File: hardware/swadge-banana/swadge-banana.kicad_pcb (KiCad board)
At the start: 2 copper layers, 85 x 173.2 mm, 46 parts, among them J1 USB_B_Micro, SW1 SW_SPDT, U1 AP1117-33, U2 ESP-13-WROOM-02D, U3 BUS_PCIexpress, U4 OLED_CONNECTOR, U5 QMA6981, U6 OLED_DISPLAY

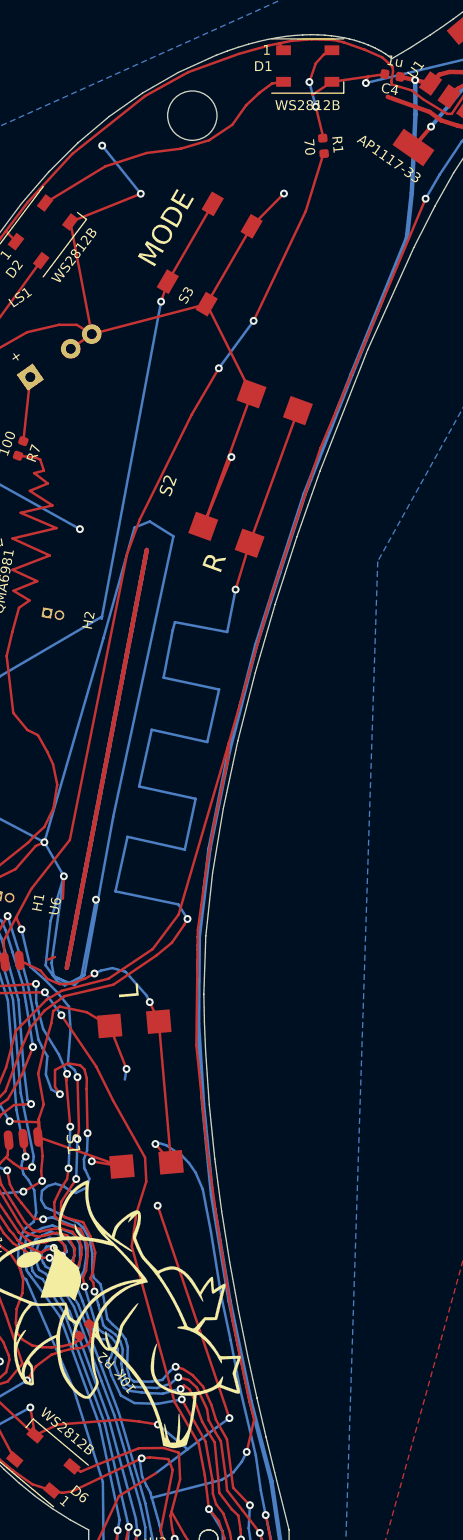
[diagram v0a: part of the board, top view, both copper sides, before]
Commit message: Readded missing batteries, filled zones
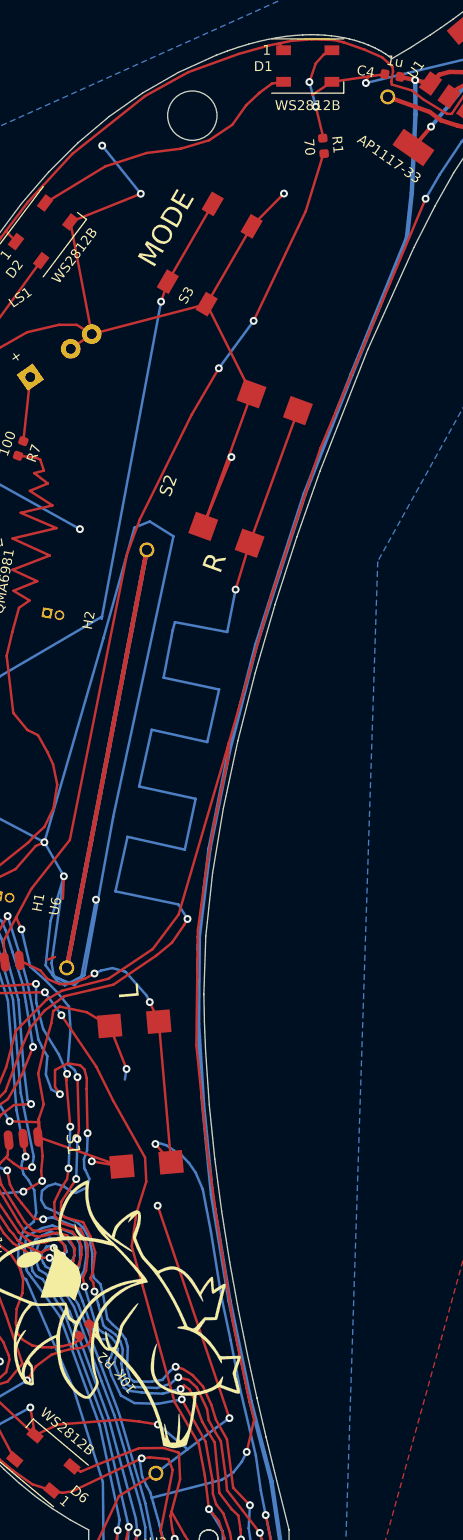
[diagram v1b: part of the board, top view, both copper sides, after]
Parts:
- added BT1: Battery, Swadge_Parts:2460, B.Cu at (137.8, 149.8)
- added BT2: Battery, Swadge_Parts:2460, B.Cu at (153.6, 58.9)

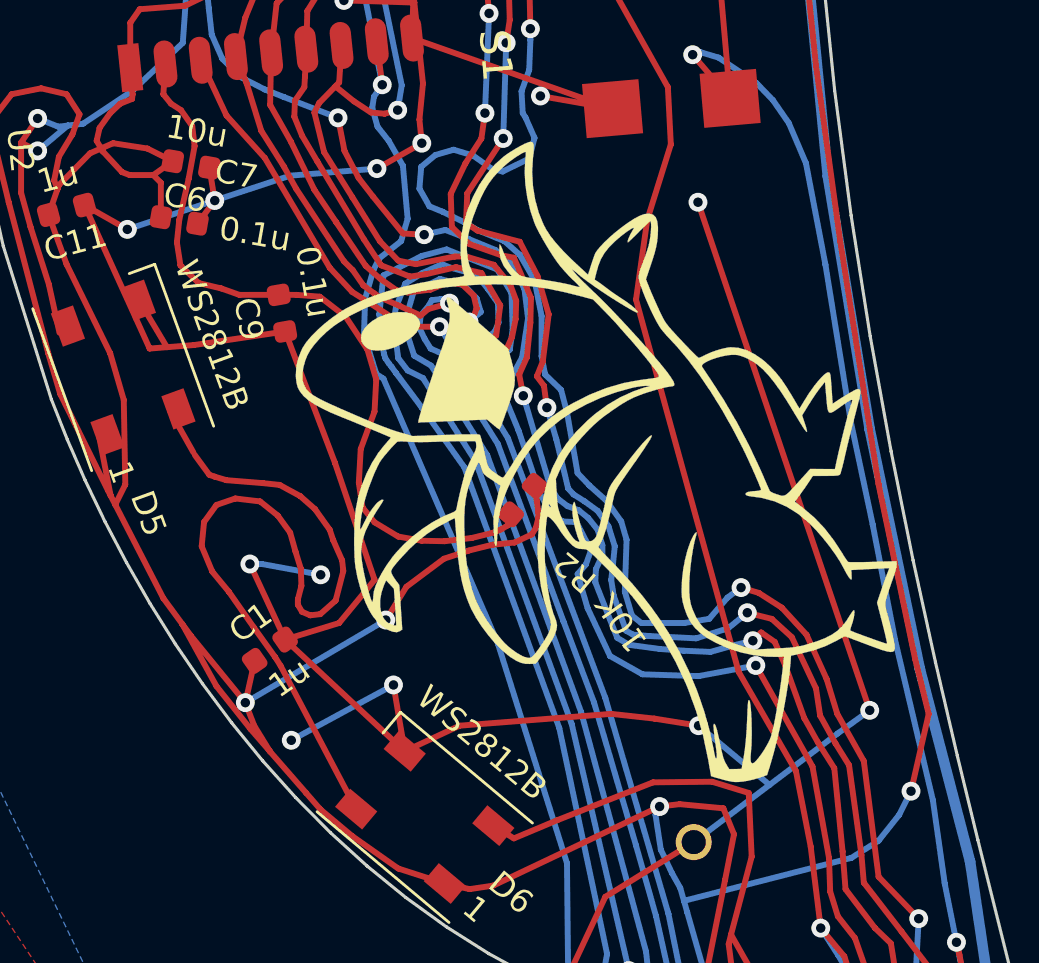
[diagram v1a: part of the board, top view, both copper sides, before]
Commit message: Added banana label to the back of the banana Rotated Lil'B on the front of the banana
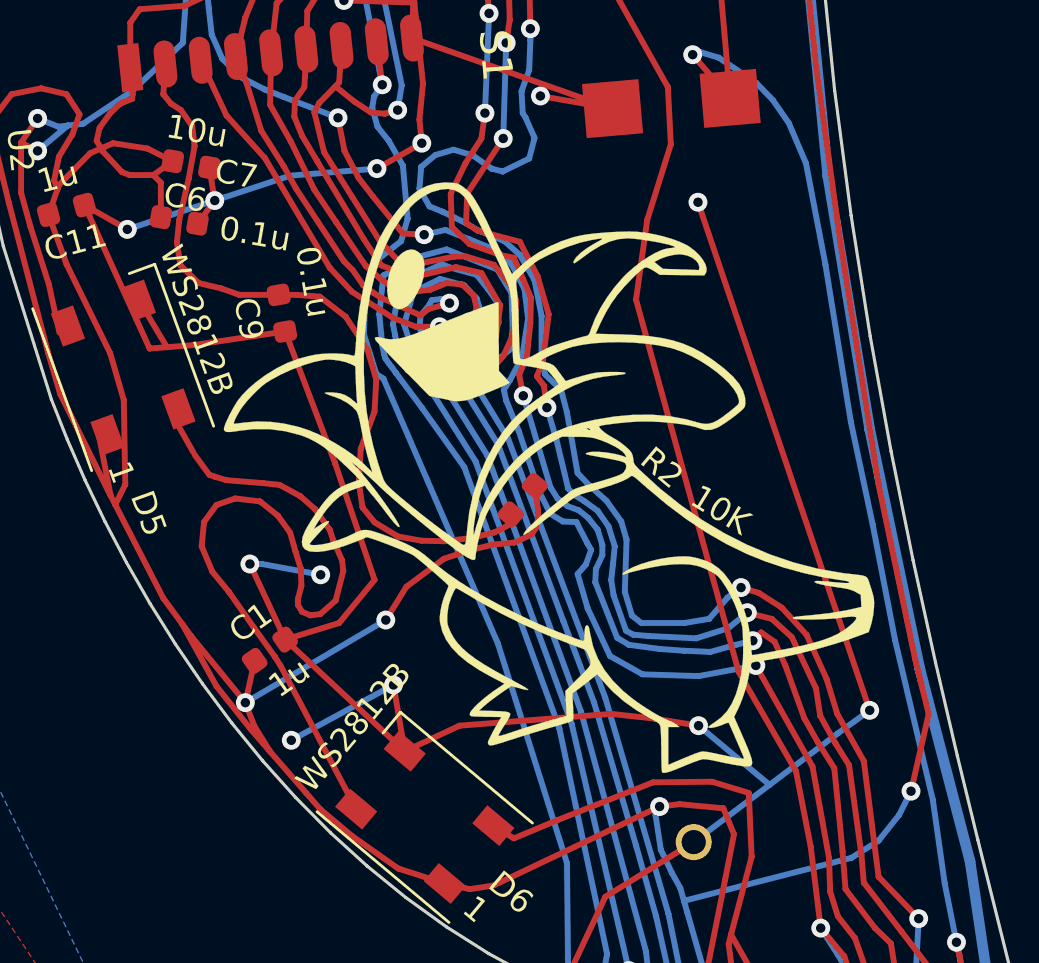
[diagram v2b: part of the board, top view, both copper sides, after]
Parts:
- removed the G*** at (125.3, 101.6)
- added Ref**: Val**, Swadge_Parts:banana-label, B.Cu at (125.4, 101.8)
- moved Ref** 2.07 mm to (136.1, 159.9), turned to 0 degrees

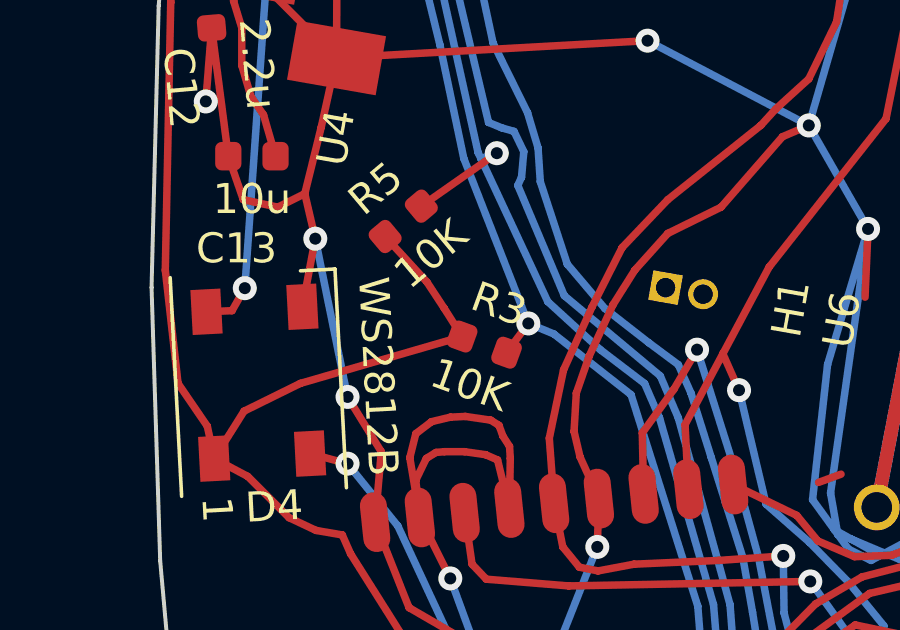
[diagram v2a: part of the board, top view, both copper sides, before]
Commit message: (Banana this time) Changed I2C pullups to 1K Updated digikey part numbers on BOM
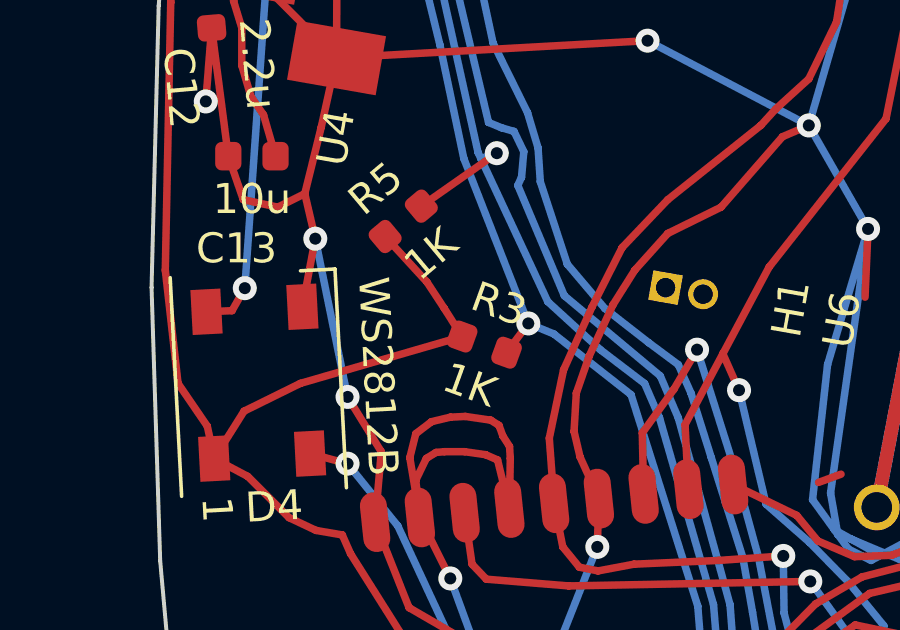
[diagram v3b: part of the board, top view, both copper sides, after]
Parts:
- R3, R5: value 10K -> 1K
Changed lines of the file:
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@@
       (effects (font (size 1 1) (thickness 0.15)))
     )
-    (fp_text value 10K (at 0 1.43 40) (layer F.SilkS)
+    (fp_text value 1K (at 0 1.43 40) (layer F.SilkS)
       (effects (font (size 1 1) (thickness 0.15)))
     )
@@
       (effects (font (size 1 1) (thickness 0.15)))
     )
-    (fp_text value 10K (at 0 1.43 160) (layer F.SilkS)
+    (fp_text value 1K (at 0 1.43 160) (layer F.SilkS)
       (effects (font (size 1 1) (thickness 0.15)))
     )
